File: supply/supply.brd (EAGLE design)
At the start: 19.7 x 52.1 mm, 14 parts, among them IC3 R-78E3.3-0.5, J1 DIN5, J2 1X2-3.5MM

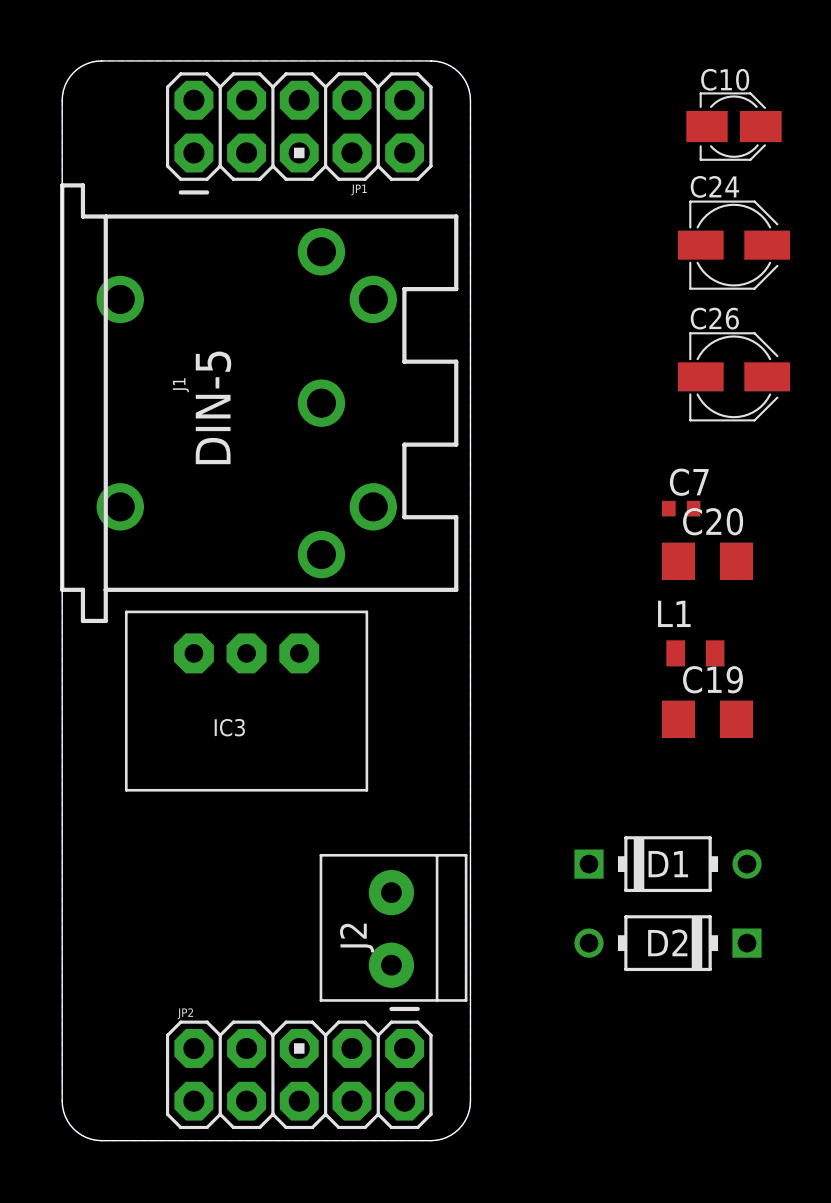
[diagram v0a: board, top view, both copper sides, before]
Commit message: Redo supply to be much simpler
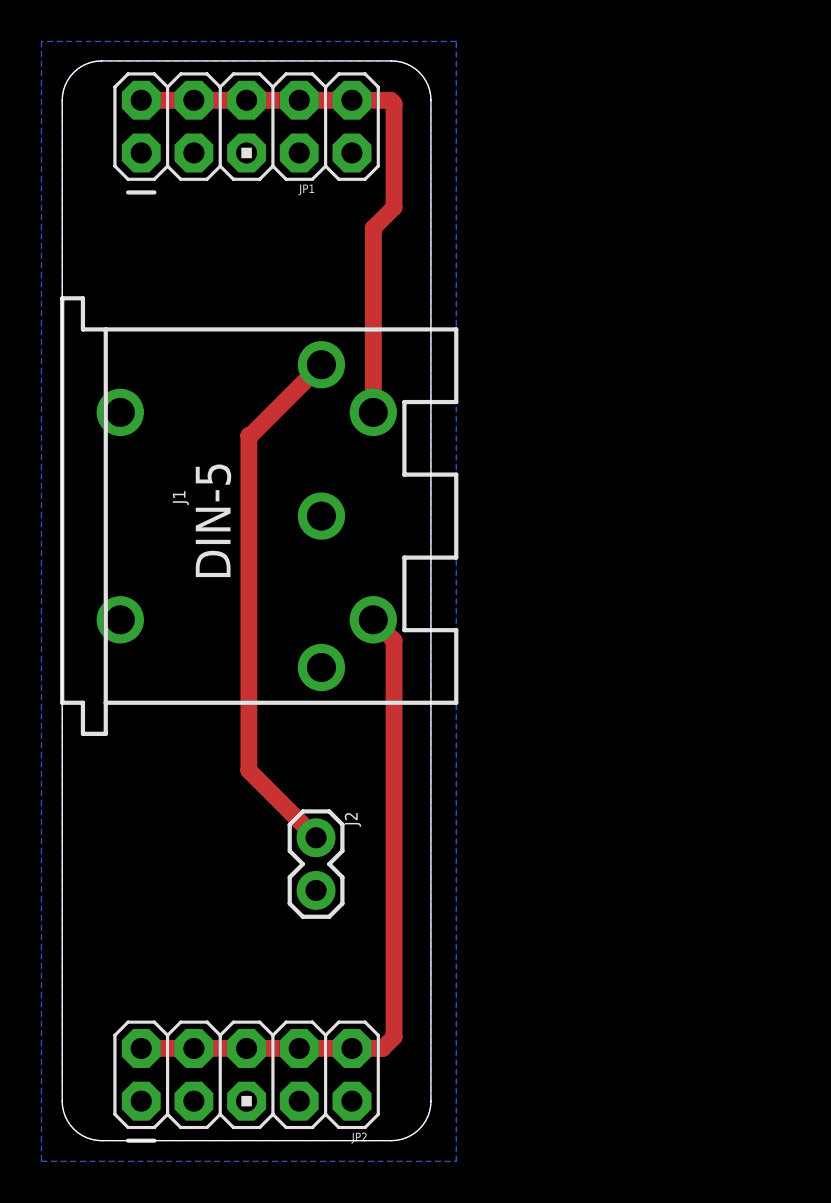
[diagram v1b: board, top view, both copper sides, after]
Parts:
- removed C10: 10u, rcl:PANASONIC_A
- removed C19, C20: 22u, rcl:C1206
- removed C24, C26: 22u, rcl:PANASONIC_B
- removed C7: 100n, rcl:C0402
- removed D1, D2: 1N4001, gm-diodes:DO41-3
- removed IC3: R-78E3.3-0.5, og-vreg:WE78
- removed L1: 33u, og-rcl:L2012C
- J2: value 1X2-3.5MM -> (none); device adafruit:1X2-3.5MM -> SparkFun-Connectors:1X02
- moved J2 5.74 mm to (12.2, 14.6), turned to 270 degrees
- moved J1 5.45 mm to (0.00, 30.1)
- moved JP1 2.54 mm to (8.89, 48.9)
- moved JP2 2.54 mm to (8.89, 3.17), turned to 90 degrees
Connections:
- removed net +3V3: C10.+, C7.1, IC3.3, J2.1
- removed net N$1: C19.1, IC3.1, L1.2
- removed net N$2: D1.A, J1.3
- removed net N$3: D2.C, J1.1
- new net +5V: J1.3, J2.1
- net GND: now also J1.1, JP2.1, JP2.3, JP2.5, JP2.7, JP2.9; no longer C10.-, C19.2, C20.2, C24.-, C26.+, C7.2, IC3.2, JP2.10, JP2.2, JP2.4, JP2.6, JP2.8
- net VCC: now also J1.5; no longer C20.1, C24.+, D1.C, L1.1
- net VEE: now also J1.4, JP2.10, JP2.2, JP2.4, JP2.6, JP2.8; no longer C26.-, D2.A, JP2.1, JP2.3, JP2.5, JP2.7, JP2.9
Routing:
- net VEE: track 0.00 -> 33.6 mm
- net VCC: track 0.00 -> 27.6 mm
- net +5V: track 0.00 -> 25.7 mm
- added copper zone on layer 16, net GND
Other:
- board size 19.7 x 52.1 mm -> 17.8 x 52.1 mm
- board text added: "+5v"
- board text added: "GND"
